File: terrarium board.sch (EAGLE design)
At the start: 30 parts

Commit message: Getting ready to send v2 to OSH Park.
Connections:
- removed net N$1: C3.1, SHIFT2.VCC
- removed net N$27: R8.1, SHIFT2.A4
- removed net N$28: R7.1, SHIFT2.A5
- removed net N$29: SPARK.D0, TEMP_HUM.DIN
- new net N$10: R6.1, SHIFT2.A1
- new net N$12: SPARK.A6, TEMP_HUM.DIN
- new net N$13: R11.1, SHIFT2.A2
- new net N$15: R10.1, SHIFT2.A3
- net +5V: now also C3.1, POWER.VCC1, POWER.VCC2, SHIFT2.VCC; no longer POWER.GND
- net GND: now also POWER.GND1, POWER.GND2; no longer POWER.VCC
- net N$23: now also R9.1, SHIFT2.A4; no longer R6.1, SHIFT1.A3
- net N$24: now also R8.1, SHIFT2.A5; no longer R11.1, SHIFT2.A1
- net N$25: now also R7.1, SHIFT2.A6; no longer R10.1, SHIFT2.A2
- net N$26: now also SHIFT2.B6; no longer R9.1, SHIFT2.A3
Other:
- moved on the sheet: BASE, C2, R6, TEMP_HUM

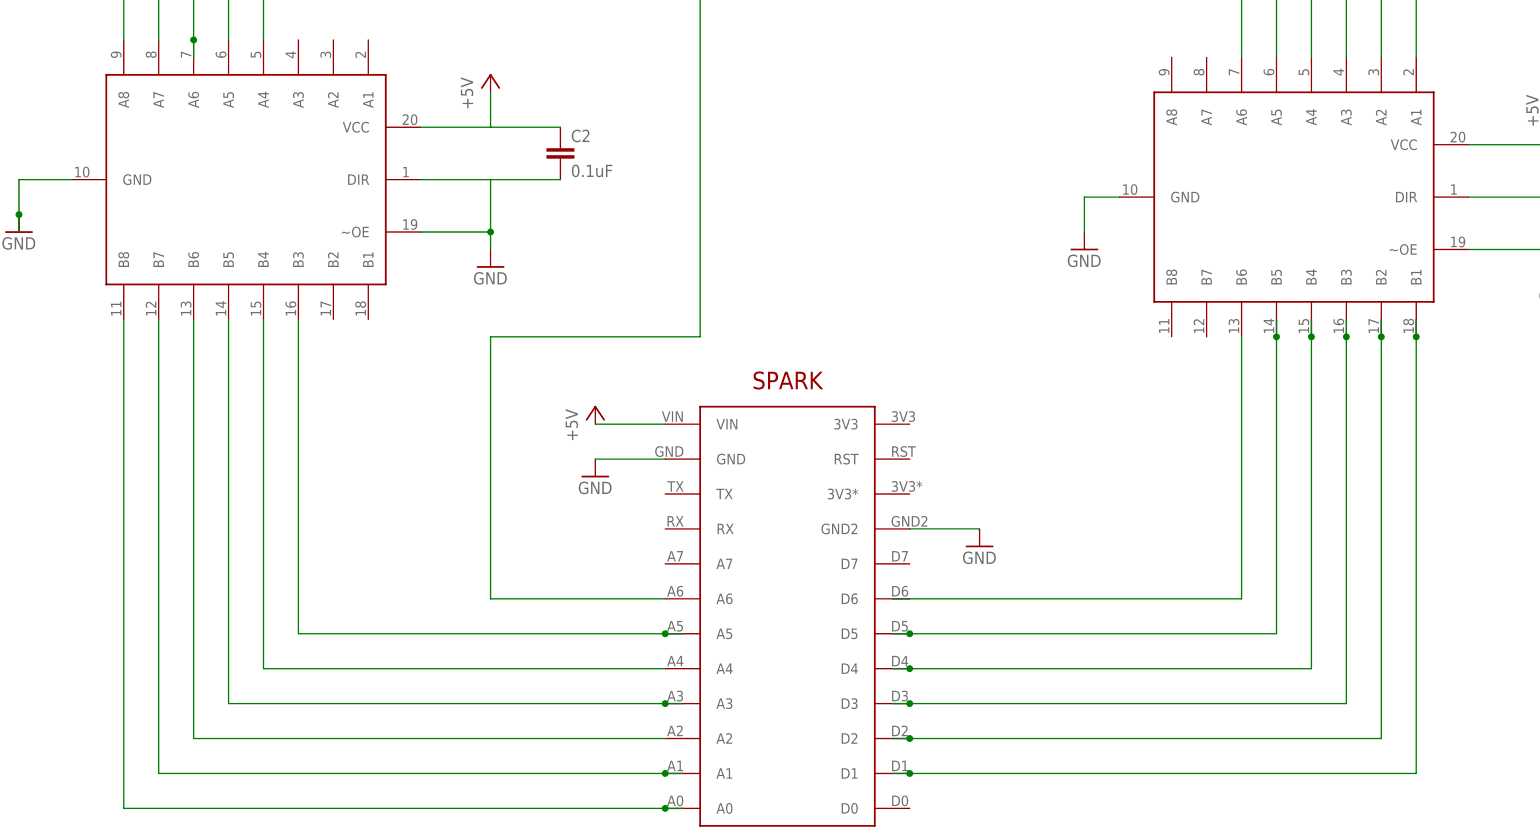
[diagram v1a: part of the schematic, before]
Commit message: Sadly, pillar0 was touching, but Eagle didn't think it was hooked up.
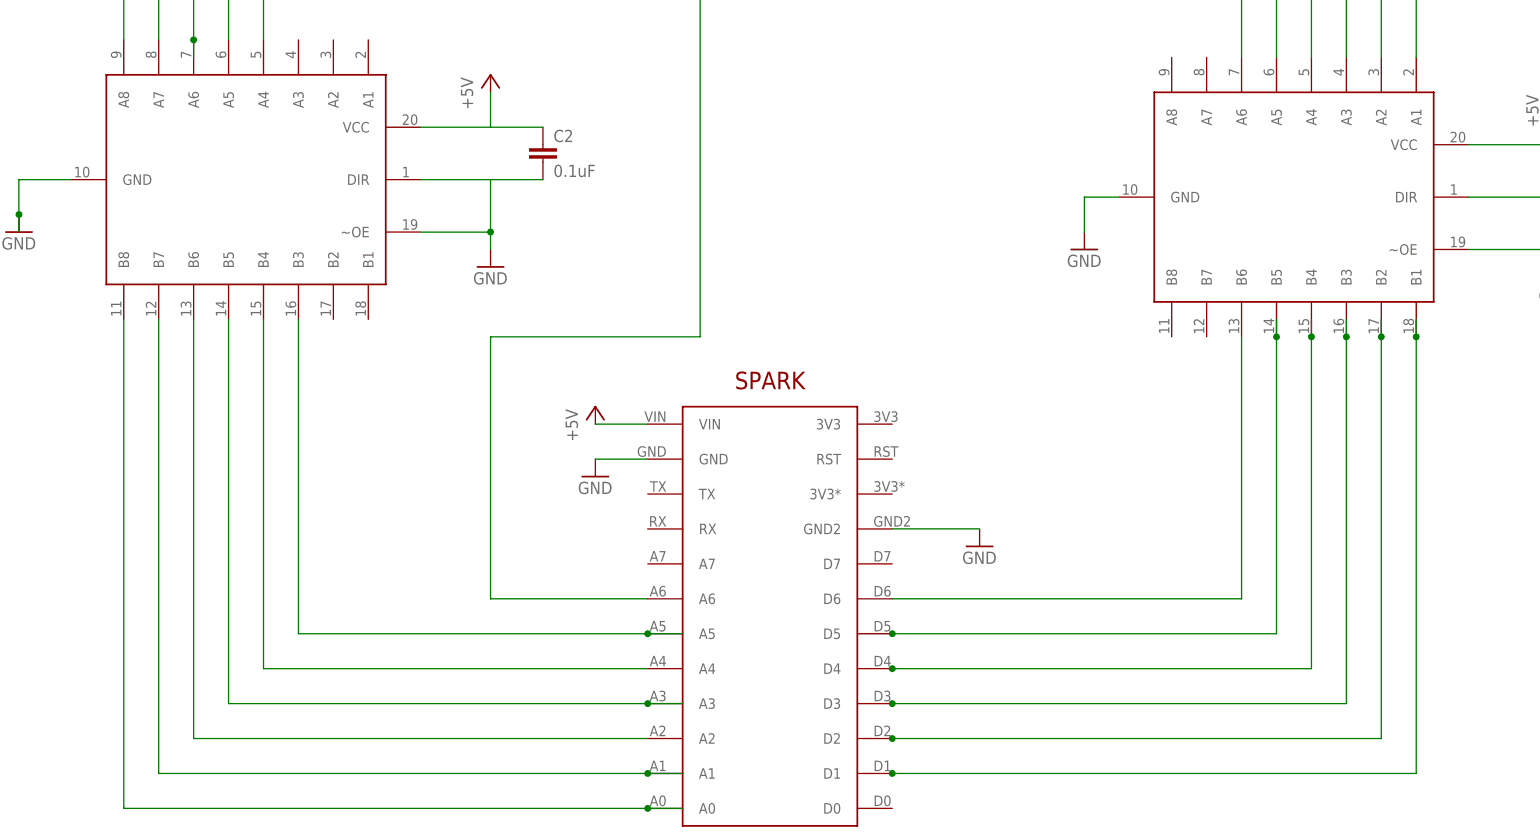
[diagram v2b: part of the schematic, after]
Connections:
- net N$26: now also SPARK.D6
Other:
- moved on the sheet: C2, SPARK
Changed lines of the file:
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@@
 <instances>
 <instance part="POWER" gate="G$1" x="121.92" y="35.56" rot="MR180"/>
-<instance part="SPARK" gate="G$1" x="320.04" y="-53.34"/>
+<instance part="SPARK" gate="G$1" x="317.5" y="-53.34"/>
 <instance part="R1" gate="G$1" x="119.38" y="101.6" rot="R90"/>
 <instance part="LED0" gate="G$1" x="119.38" y="129.54"/>
@@
 <instance part="GND14" gate="1" x="363.22" y="-10.16"/>
 <instance part="GND19" gate="1" x="208.28" y="-7.62"/>
-<instance part="C2" gate="G$1" x="287.02" y="2.54"/>
+<instance part="C2" gate="G$1" x="284.48" y="2.54"/>
 <instance part="C3" gate="G$1" x="436.88" y="0"/>
 <instance part="R7" gate="G$1" x="317.5" y="106.68" rot="R90"/>
@@
 <segment>
 <pinref part="SPARK" gate="G$1" pin="VIN"/>
-<wire x1="302.26" y1="-35.56" x2="292.1" y2="-35.56" width="0.1524" layer="91"/>
+<wire x1="299.72" y1="-35.56" x2="292.1" y2="-35.56" width="0.1524" layer="91"/>
 <pinref part="P+15" gate="1" pin="+5V"/>
 </segment>
@@
 <wire x1="276.86" y1="7.62" x2="266.7" y2="7.62" width="0.1524" layer="91"/>
 <pinref part="C2" gate="G$1" pin="1"/>
-<wire x1="276.86" y1="7.62" x2="287.02" y2="7.62" width="0.1524" layer="91"/>
+<wire x1="276.86" y1="7.62" x2="284.48" y2="7.62" width="0.1524" layer="91"/>
 <pinref part="SHIFT1" gate="G$1" pin="VCC"/>
 </segment>
@@
 <pinref part="SPARK" gate="G$1" pin="GND"/>
 <pinref part="GND17" gate="1" pin="GND"/>
-<wire x1="302.26" y1="-40.64" x2="292.1" y2="-40.64" width="0.1524" layer="91"/>
+<wire x1="299.72" y1="-40.64" x2="292.1" y2="-40.64" width="0.1524" layer="91"/>
 </segment>
 <segment>
 <pinref part="SPARK" gate="G$1" pin="GND2"/>
 <pinref part="GND16" gate="1" pin="GND"/>
-<wire x1="337.82" y1="-50.8" x2="347.98" y2="-50.8" width="0.1524" layer="91"/>
+<wire x1="335.28" y1="-50.8" x2="347.98" y2="-50.8" width="0.1524" layer="91"/>
 </segment>
 <segment>
@@
 <junction x="276.86" y="-7.62"/>
 <pinref part="C2" gate="G$1" pin="2"/>
-<wire x1="287.02" y1="0" x2="276.86" y2="0" width="0.1524" layer="91"/>
+<wire x1="284.48" y1="0" x2="276.86" y2="0" width="0.1524" layer="91"/>
 <pinref part="SHIFT1" gate="G$1" pin="DIR"/>
 <pinref part="SHIFT1" gate="G$1" pin="~OE"/>
@@
 <net name="N$30" class="0">
 <segment>
-<wire x1="335.28" y1="-86.36" x2="337.82" y2="-86.36" width="0.1524" layer="91"/>
-<wire x1="337.82" y1="-86.36" x2="411.48" y2="-86.36" width="0.1524" layer="91"/>
+<wire x1="335.28" y1="-86.36" x2="411.48" y2="-86.36" width="0.1524" layer="91"/>
 <wire x1="411.48" y1="-86.36" x2="411.48" y2="-22.86" width="0.1524" layer="91"/>
 <pinref part="SHIFT2" gate="G$1" pin="B1"/>
@@
 <junction x="411.48" y="-22.86"/>
 <pinref part="SPARK" gate="G$1" pin="D1"/>
-<junction x="337.82" y="-86.36"/>
+<junction x="335.28" y="-86.36"/>
 </segment>
 </net>
 <net name="N$33" class="0">
 <segment>
-<wire x1="335.28" y1="-71.12" x2="337.82" y2="-71.12" width="0.1524" layer="91"/>
-<wire x1="337.82" y1="-71.12" x2="396.24" y2="-71.12" width="0.1524" layer="91"/>
+<wire x1="335.28" y1="-71.12" x2="396.24" y2="-71.12" width="0.1524" layer="91"/>
 <wire x1="396.24" y1="-71.12" x2="396.24" y2="-22.86" width="0.1524" layer="91"/>
 <pinref part="SHIFT2" gate="G$1" pin="B4"/>
@@
 <junction x="396.24" y="-22.86"/>
 <pinref part="SPARK" gate="G$1" pin="D4"/>
-<junction x="337.82" y="-71.12"/>
+<junction x="335.28" y="-71.12"/>
 </segment>
 </net>
 <net name="N$2" class="0">
 <segment>
-<wire x1="335.28" y1="-81.28" x2="337.82" y2="-81.28" width="0.1524" layer="91"/>
-<wire x1="337.82" y1="-81.28" x2="406.4" y2="-81.28" width="0.1524" layer="91"/>
+<wire x1="335.28" y1="-81.28" x2="406.4" y2="-81.28" width="0.1524" layer="91"/>
 <wire x1="406.4" y1="-81.28" x2="406.4" y2="-22.86" width="0.1524" layer="91"/>
 <pinref part="SHIFT2" gate="G$1" pin="B2"/>
@@
 <junction x="406.4" y="-22.86"/>
 <pinref part="SPARK" gate="G$1" pin="D2"/>
-<junction x="337.82" y="-81.28"/>
+<junction x="335.28" y="-81.28"/>
 </segment>
 </net>
 <net name="N$31" class="0">
 <segment>
-<wire x1="335.28" y1="-76.2" x2="337.82" y2="-76.2" width="0.1524" layer="91"/>
-<wire x1="337.82" y1="-76.2" x2="401.32" y2="-76.2" width="0.1524" layer="91"/>
+<wire x1="335.28" y1="-76.2" x2="401.32" y2="-76.2" width="0.1524" layer="91"/>
 <wire x1="401.32" y1="-76.2" x2="401.32" y2="-22.86" width="0.1524" layer="91"/>
 <pinref part="SHIFT2" gate="G$1" pin="B3"/>
@@
 <junction x="401.32" y="-22.86"/>
 <pinref part="SPARK" gate="G$1" pin="D3"/>
-<junction x="337.82" y="-76.2"/>
+<junction x="335.28" y="-76.2"/>
 </segment>
 </net>
 <net name="N$32" class="0">
 <segment>
-<wire x1="335.28" y1="-66.04" x2="337.82" y2="-66.04" width="0.1524" layer="91"/>
-<wire x1="337.82" y1="-66.04" x2="391.16" y2="-66.04" width="0.1524" layer="91"/>
+<wire x1="335.28" y1="-66.04" x2="391.16" y2="-66.04" width="0.1524" layer="91"/>
 <wire x1="391.16" y1="-66.04" x2="391.16" y2="-22.86" width="0.1524" layer="91"/>
 <pinref part="SHIFT2" gate="G$1" pin="B5"/>
@@
 <junction x="391.16" y="-22.86"/>
 <pinref part="SPARK" gate="G$1" pin="D5"/>
-<junction x="337.82" y="-66.04"/>
+<junction x="335.28" y="-66.04"/>
 </segment>
 </net>
 <net name="N$34" class="0">
 <segment>
-<wire x1="304.8" y1="-91.44" x2="302.26" y2="-91.44" width="0.1524" layer="91"/>
-<wire x1="302.26" y1="-91.44" x2="223.52" y2="-91.44" width="0.1524" layer="91"/>
+<wire x1="304.8" y1="-91.44" x2="299.72" y2="-91.44" width="0.1524" layer="91"/>
+<wire x1="299.72" y1="-91.44" x2="223.52" y2="-91.44" width="0.1524" layer="91"/>
 <wire x1="223.52" y1="-91.44" x2="223.52" y2="-20.32" width="0.1524" layer="91"/>
 <pinref part="SHIFT1" gate="G$1" pin="B8"/>
 <pinref part="SPARK" gate="G$1" pin="A0"/>
-<junction x="302.26" y="-91.44"/>
+<junction x="299.72" y="-91.44"/>
 </segment>
 </net>
 <net name="N$35" class="0">
 <segment>
-<wire x1="304.8" y1="-86.36" x2="302.26" y2="-86.36" width="0.1524" layer="91"/>
-<wire x1="302.26" y1="-86.36" x2="228.6" y2="-86.36" width="0.1524" layer="91"/>
+<wire x1="304.8" y1="-86.36" x2="299.72" y2="-86.36" width="0.1524" layer="91"/>
+<wire x1="299.72" y1="-86.36" x2="228.6" y2="-86.36" width="0.1524" layer="91"/>
 <wire x1="228.6" y1="-86.36" x2="228.6" y2="-20.32" width="0.1524" layer="91"/>
 <pinref part="SHIFT1" gate="G$1" pin="B7"/>
 <pinref part="SPARK" gate="G$1" pin="A1"/>
-<junction x="302.26" y="-86.36"/>
+<junction x="299.72" y="-86.36"/>
 </segment>
 </net>
@@
 <segment>
 <pinref part="SPARK" gate="G$1" pin="A2"/>
-<wire x1="302.26" y1="-81.28" x2="233.68" y2="-81.28" width="0.1524" layer="91"/>
+<wire x1="299.72" y1="-81.28" x2="233.68" y2="-81.28" width="0.1524" layer="91"/>
 <wire x1="233.68" y1="-81.28" x2="233.68" y2="-20.32" width="0.1524" layer="91"/>
 <pinref part="SHIFT1" gate="G$1" pin="B6"/>
@@
 <net name="N$37" class="0">
 <segment>
-<wire x1="304.8" y1="-76.2" x2="302.26" y2="-76.2" width="0.1524" layer="91"/>
-<wire x1="302.26" y1="-76.2" x2="238.76" y2="-76.2" width="0.1524" layer="91"/>
+<wire x1="304.8" y1="-76.2" x2="299.72" y2="-76.2" width="0.1524" layer="91"/>
+<wire x1="299.72" y1="-76.2" x2="238.76" y2="-76.2" width="0.1524" layer="91"/>
 <wire x1="238.76" y1="-76.2" x2="238.76" y2="-20.32" width="0.1524" layer="91"/>
 <pinref part="SHIFT1" gate="G$1" pin="B5"/>
 <pinref part="SPARK" gate="G$1" pin="A3"/>
-<junction x="302.26" y="-76.2"/>
+<junction x="299.72" y="-76.2"/>
 </segment>
 </net>
@@
 <segment>
 <pinref part="SPARK" gate="G$1" pin="A4"/>
-<wire x1="302.26" y1="-71.12" x2="243.84" y2="-71.12" width="0.1524" layer="91"/>
+<wire x1="299.72" y1="-71.12" x2="243.84" y2="-71.12" width="0.1524" layer="91"/>
 <wire x1="243.84" y1="-71.12" x2="243.84" y2="-20.32" width="0.1524" layer="91"/>
 <pinref part="SHIFT1" gate="G$1" pin="B4"/>
@@
 <net name="N$39" class="0">
 <segment>
-<wire x1="304.8" y1="-66.04" x2="302.26" y2="-66.04" width="0.1524" layer="91"/>
-<wire x1="302.26" y1="-66.04" x2="248.92" y2="-66.04" width="0.1524" layer="91"/>
+<wire x1="304.8" y1="-66.04" x2="299.72" y2="-66.04" width="0.1524" layer="91"/>
+<wire x1="299.72" y1="-66.04" x2="248.92" y2="-66.04" width="0.1524" layer="91"/>
 <wire x1="248.92" y1="-66.04" x2="248.92" y2="-20.32" width="0.1524" layer="91"/>
 <pinref part="SHIFT1" gate="G$1" pin="B3"/>
 <pinref part="SPARK" gate="G$1" pin="A5"/>
-<junction x="302.26" y="-66.04"/>
+<junction x="299.72" y="-66.04"/>
 </segment>
 </net>
@@
 <wire x1="276.86" y1="-22.86" x2="276.86" y2="-60.96" width="0.1524" layer="91"/>
 <pinref part="SPARK" gate="G$1" pin="A6"/>
-<wire x1="276.86" y1="-60.96" x2="302.26" y2="-60.96" width="0.1524" layer="91"/>
+<wire x1="276.86" y1="-60.96" x2="299.72" y2="-60.96" width="0.1524" layer="91"/>
 </segment>
 </net>
@@
 <wire x1="386.08" y1="-22.86" x2="386.08" y2="-60.96" width="0.1524" layer="91"/>
 <wire x1="386.08" y1="-60.96" x2="335.28" y2="-60.96" width="0.1524" layer="91"/>
-</segment>
-</net>
+<pinref part="SPARK" gate="G$1" pin="D6"/>
+</segment>
+</net>

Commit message: Fixed issues from v2.
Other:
- moved on the sheet: POWER
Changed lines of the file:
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@@
 <class number="0" name="default" width="0" drill="0">
 </class>
-<class number="1" name="power" width="3.556" drill="0">
+<class number="1" name="power" width="1.524" drill="0">
 </class>
 </classes>
@@
 </plain>
 <instances>
-<instance part="POWER" gate="G$1" x="121.92" y="35.56" rot="MR180"/>
+<instance part="POWER" gate="G$1" x="119.38" y="35.56" rot="MR180"/>
 <instance part="SPARK" gate="G$1" x="317.5" y="-53.34"/>
 <instance part="R1" gate="G$1" x="119.38" y="101.6" rot="R90"/>
@@
 <instance part="GND11" gate="1" x="421.64" y="109.22"/>
 <instance part="GND12" gate="1" x="254" y="109.22"/>
-<instance part="GND13" gate="1" x="431.8" y="-15.24"/>
+<instance part="GND13" gate="1" x="431.8" y="-20.32"/>
 <instance part="GND15" gate="1" x="137.16" y="22.86"/>
 <instance part="GND16" gate="1" x="347.98" y="-53.34"/>
@@
 <pinref part="C1" gate="G$1" pin="+"/>
 <wire x1="144.78" y1="40.64" x2="144.78" y2="38.1" width="0.1524" layer="91"/>
-<wire x1="134.62" y1="40.64" x2="137.16" y2="40.64" width="0.1524" layer="91"/>
+<wire x1="132.08" y1="40.64" x2="137.16" y2="40.64" width="0.1524" layer="91"/>
 <pinref part="POWER" gate="G$1" pin="VCC1"/>
 <pinref part="POWER" gate="G$1" pin="VCC2"/>
-<wire x1="134.62" y1="43.18" x2="137.16" y2="43.18" width="0.1524" layer="91"/>
+<wire x1="132.08" y1="43.18" x2="137.16" y2="43.18" width="0.1524" layer="91"/>
+<junction x="137.16" y="43.18"/>
+<junction x="137.16" y="40.64"/>
 </segment>
 <segment>
@@
 <wire x1="276.86" y1="7.62" x2="284.48" y2="7.62" width="0.1524" layer="91"/>
 <pinref part="SHIFT1" gate="G$1" pin="VCC"/>
+<junction x="276.86" y="7.62"/>
 </segment>
 <segment>
@@
 <pinref part="SHIFT2" gate="G$1" pin="VCC"/>
 <pinref part="P+16" gate="1" pin="+5V"/>
+<junction x="431.8" y="5.08"/>
 </segment>
 </net>
@@
 <pinref part="SHIFT1" gate="G$1" pin="DIR"/>
 <pinref part="SHIFT1" gate="G$1" pin="~OE"/>
+<junction x="276.86" y="0"/>
 </segment>
 <segment>
@@
 <wire x1="431.8" y1="-2.54" x2="431.8" y2="-10.16" width="0.1524" layer="91"/>
 <pinref part="SHIFT2" gate="G$1" pin="~OE"/>
-<wire x1="431.8" y1="-10.16" x2="431.8" y2="-12.7" width="0.1524" layer="91"/>
 <wire x1="419.1" y1="-10.16" x2="431.8" y2="-10.16" width="0.1524" layer="91"/>
-<wire x1="431.8" y1="-10.16" x2="431.8" y2="-15.24" width="0.1524" layer="91"/>
+<wire x1="431.8" y1="-10.16" x2="431.8" y2="-17.78" width="0.1524" layer="91"/>
 <junction x="431.8" y="-10.16"/>
 <pinref part="C3" gate="G$1" pin="2"/>
 <wire x1="431.8" y1="-2.54" x2="436.88" y2="-2.54" width="0.1524" layer="91"/>
+<junction x="431.8" y="-2.54"/>
 </segment>
 <segment>
@@
 <pinref part="POWER" gate="G$1" pin="GND2"/>
 <pinref part="C1" gate="G$1" pin="-"/>
-<wire x1="134.62" y1="30.48" x2="137.16" y2="30.48" width="0.1524" layer="91"/>
+<wire x1="132.08" y1="30.48" x2="137.16" y2="30.48" width="0.1524" layer="91"/>
 <pinref part="POWER" gate="G$1" pin="GND1"/>
 <wire x1="137.16" y1="30.48" x2="144.78" y2="30.48" width="0.1524" layer="91"/>
-<wire x1="134.62" y1="27.94" x2="137.16" y2="27.94" width="0.1524" layer="91"/>
+<wire x1="132.08" y1="27.94" x2="137.16" y2="27.94" width="0.1524" layer="91"/>
 <wire x1="137.16" y1="27.94" x2="137.16" y2="30.48" width="0.1524" layer="91"/>
 <pinref part="GND15" gate="1" pin="GND"/>
 <wire x1="137.16" y1="27.94" x2="137.16" y2="25.4" width="0.1524" layer="91"/>
+<junction x="137.16" y="30.48"/>
+<junction x="137.16" y="27.94"/>
 </segment>
 </net>
